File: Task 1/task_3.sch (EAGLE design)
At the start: 6 parts

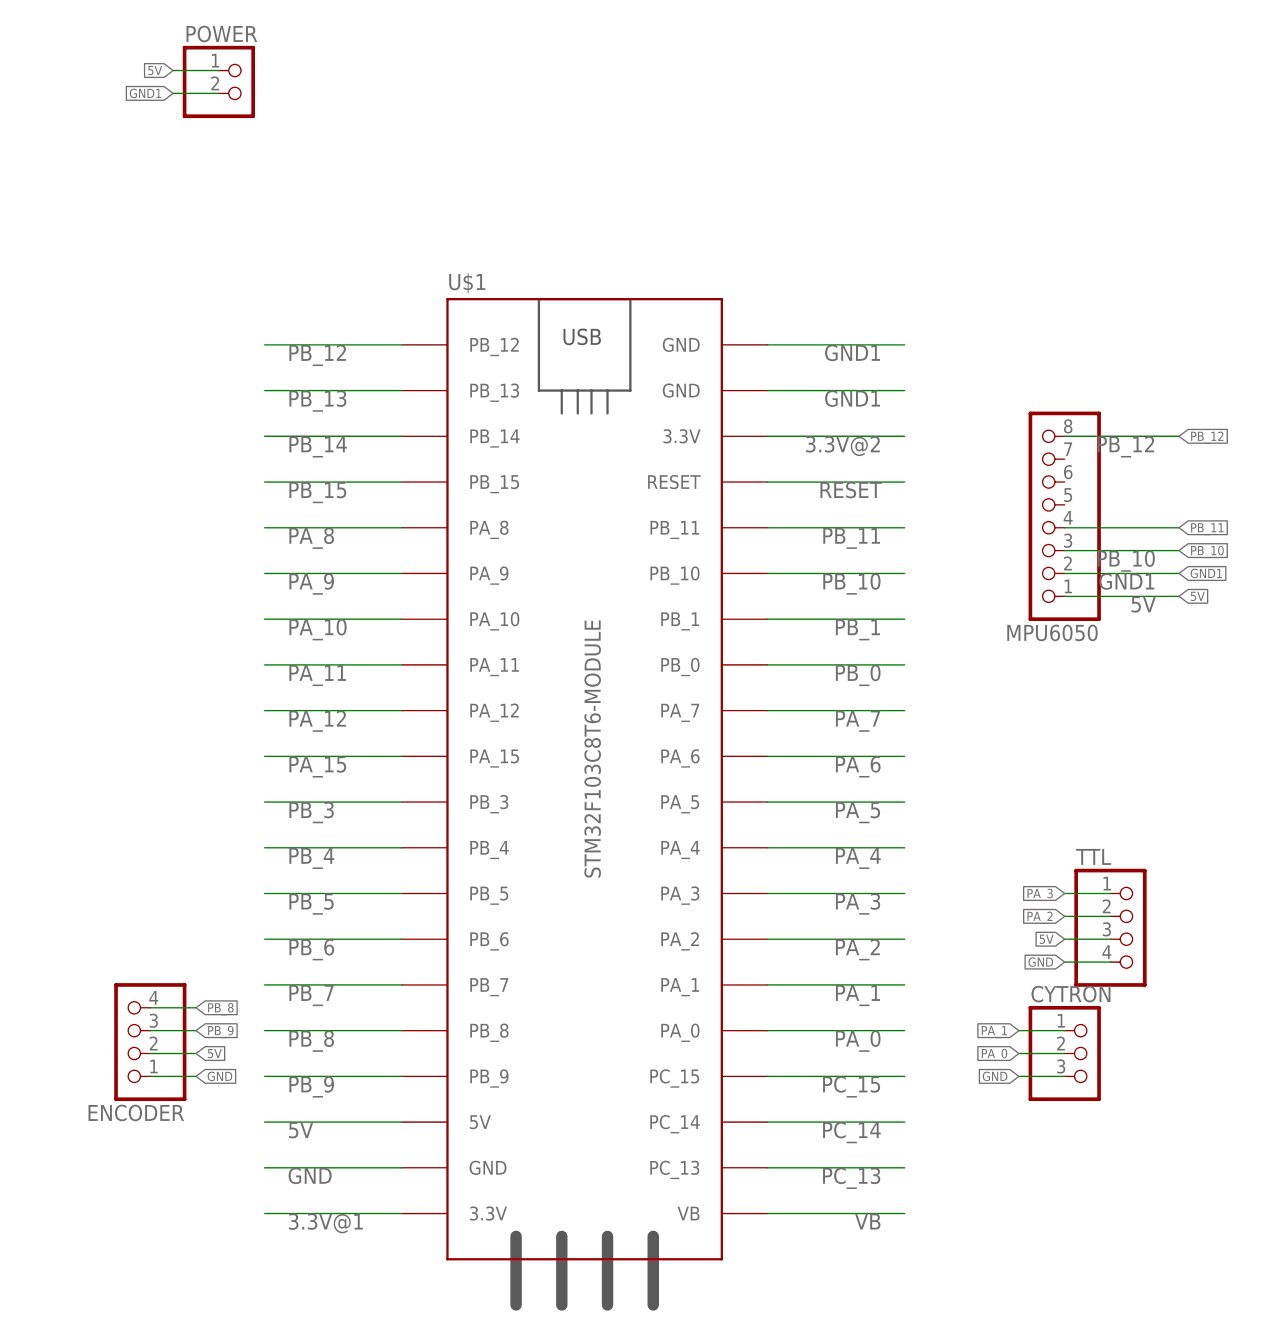
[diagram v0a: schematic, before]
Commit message: added second ttl and used correct data pinheads
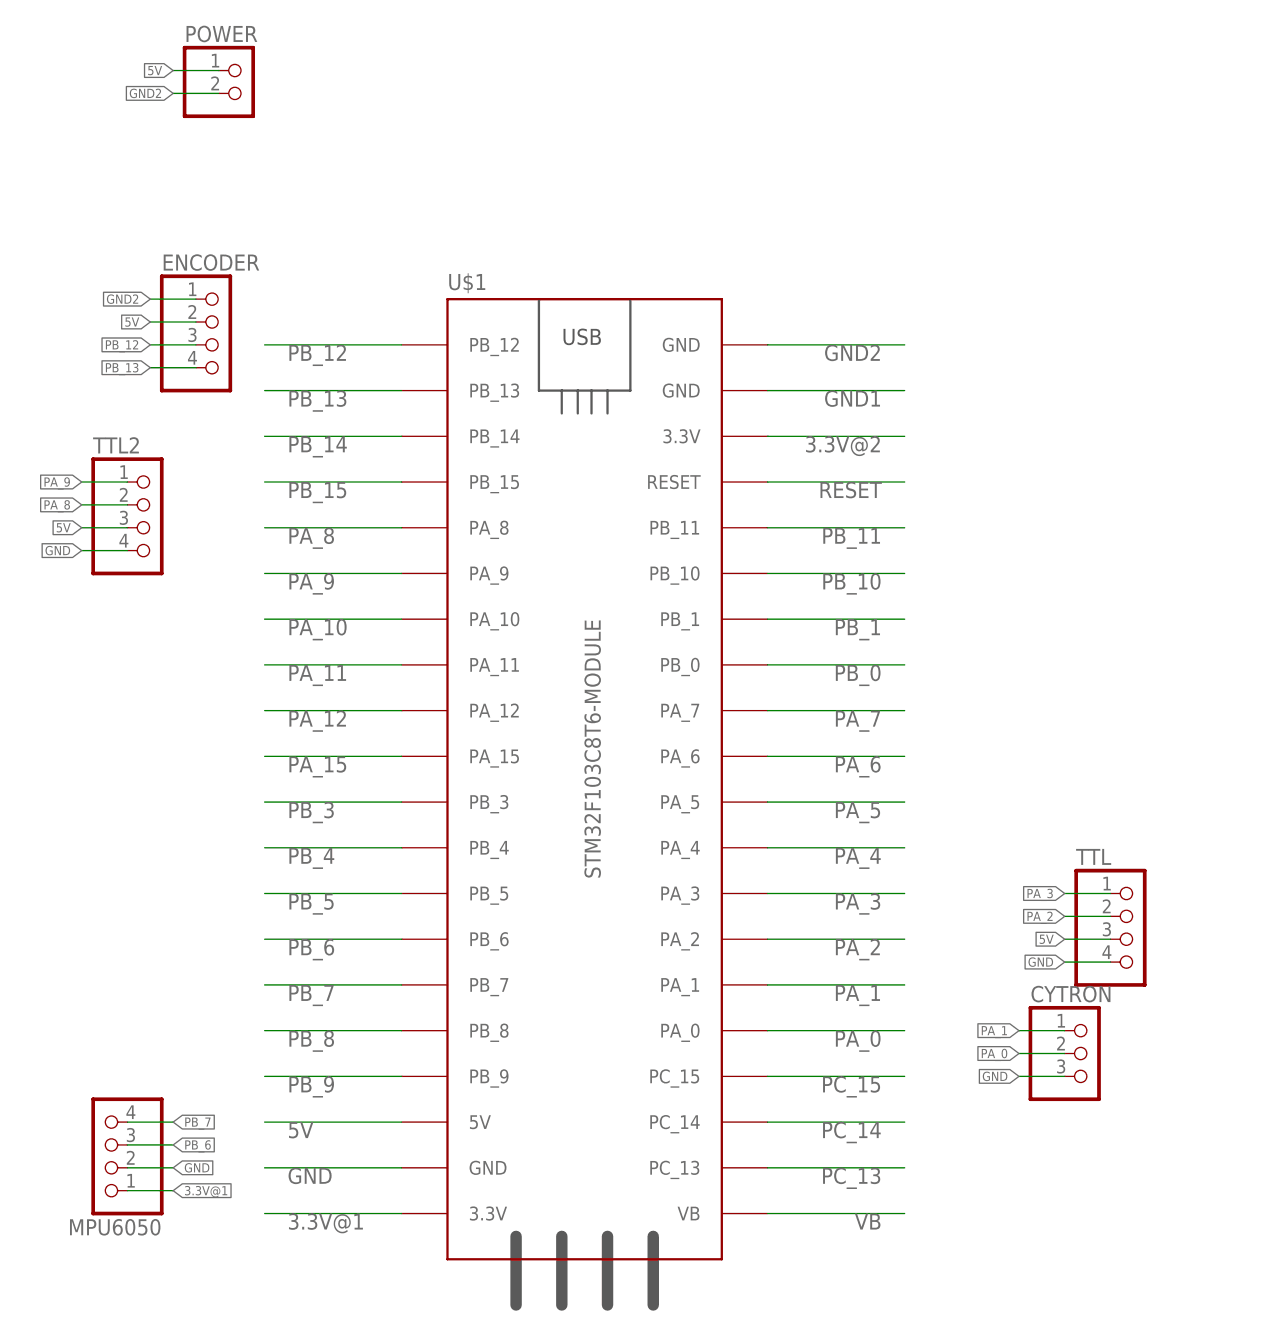
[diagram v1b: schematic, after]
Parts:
- added TTL2: (no value), MIA_LIBRARY-2-2-2:PINHD-4_DATA
- CYTRON: device MIA_LIBRARY-2-2-2:PINHD-1X3 -> MIA_LIBRARY-2-2-2:PINHD-3_DATA
- ENCODER, TTL: device MIA_LIBRARY-2-2-2:PINHD-1X4 -> MIA_LIBRARY-2-2-2:PINHD-4_DATA
- MPU6050: device MIA_LIBRARY-2-2-2:PINHD-1X8 -> MIA_LIBRARY-2-2-2:PINHD-4_DATA
- POWER: device MIA_LIBRARY-2-2-2:PINHD-1X2 -> MIA_LIBRARY-2-2-2:PINHD-2_DATA
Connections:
- new net GND2: ENCODER.1, POWER.2, U$1.GND@3
- net 3.3V@1: now also MPU6050.1
- net 5V: now also TTL2.3; no longer MPU6050.1
- net GND: now also MPU6050.2, TTL2.4; no longer ENCODER.1
- net GND1: no longer MPU6050.2, POWER.2, U$1.GND@3
- net PA_8: now also TTL2.2
- net PA_9: now also TTL2.1
- net PB_10: no longer MPU6050.3
- net PB_11: no longer MPU6050.4
- net PB_12: now also ENCODER.3; no longer MPU6050.8
- net PB_13: now also ENCODER.4
- net PB_6: now also MPU6050.3
- net PB_7: now also MPU6050.4
- net PB_8: no longer ENCODER.4
- net PB_9: no longer ENCODER.3
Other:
- moved on the sheet: ENCODER

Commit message: fixed pin configuration and routing errors, and also updated dimensions and added vias
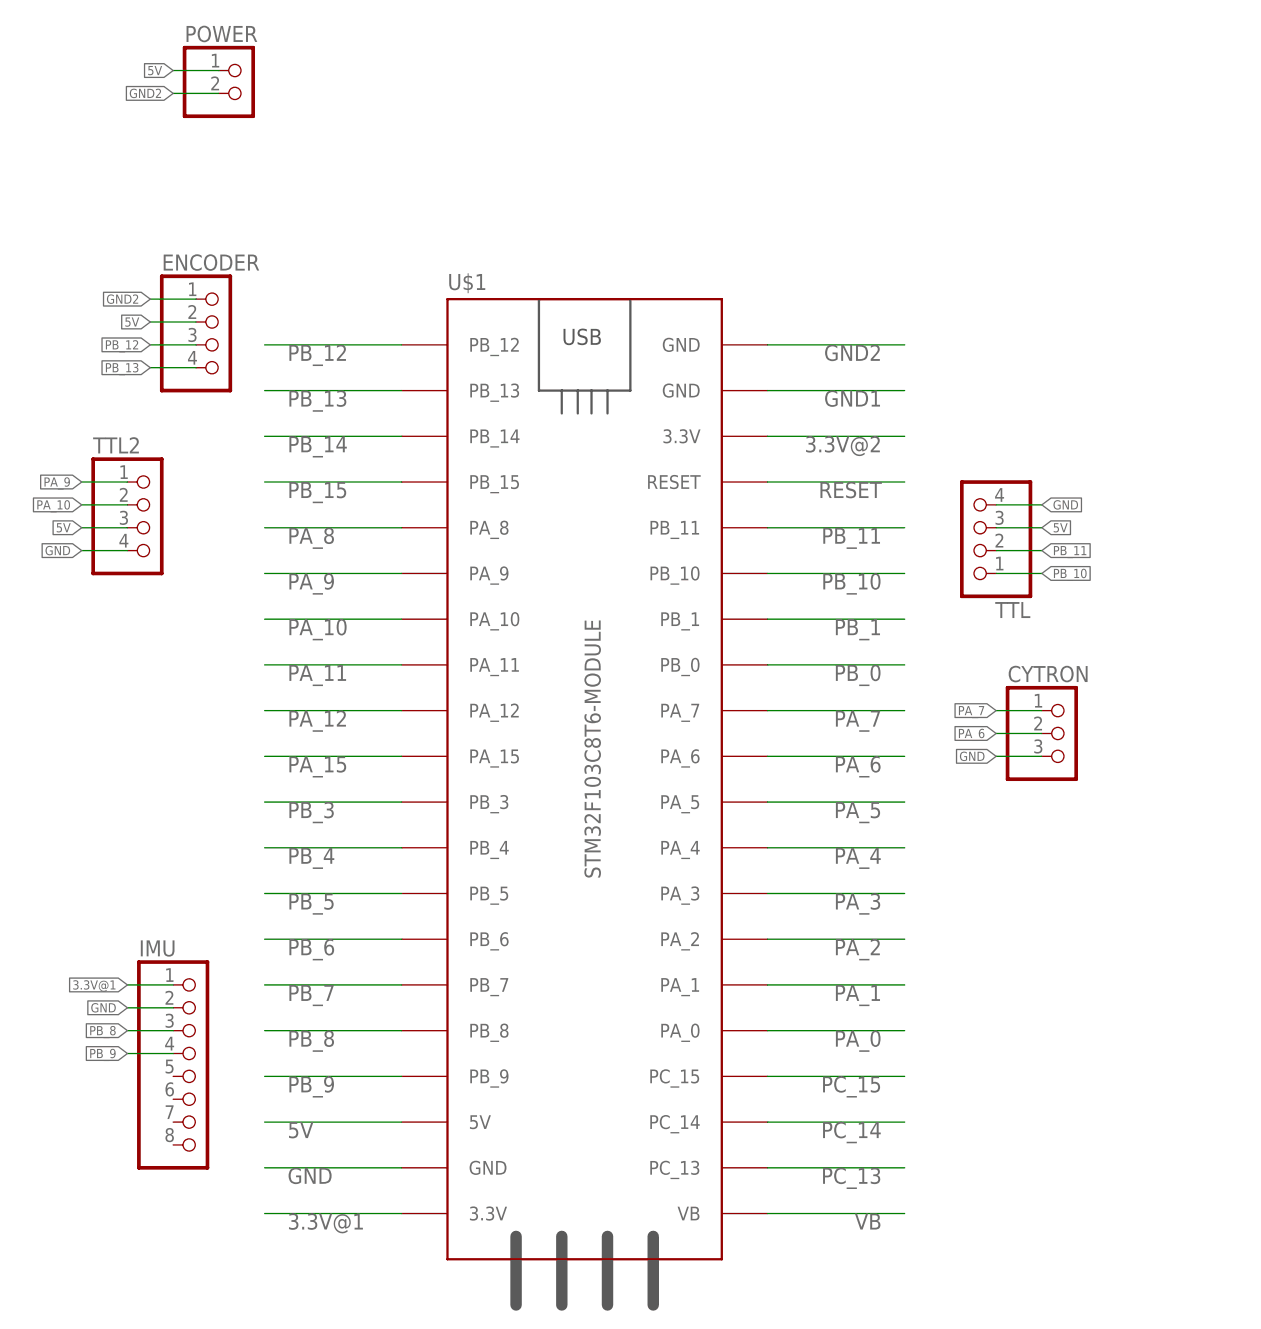
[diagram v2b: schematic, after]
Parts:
- removed MPU6050: (no value), MIA_LIBRARY-2-2-2:PINHD-4_DATA
- added IMU: (no value), MIA_LIBRARY-2-2-2:PINHD-1X8
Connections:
- net 3.3V@1: now also IMU.1; no longer MPU6050.1
- net GND: now also IMU.2; no longer MPU6050.2
- net PA_0: no longer CYTRON.2
- net PA_1: no longer CYTRON.1
- net PA_10: now also TTL2.2
- net PA_2: no longer TTL.2
- net PA_3: no longer TTL.1
- net PA_6: now also CYTRON.2
- net PA_7: now also CYTRON.1
- net PA_8: no longer TTL2.2
- net PB_10: now also TTL.1
- net PB_11: now also TTL.2
- net PB_6: no longer MPU6050.3
- net PB_7: no longer MPU6050.4
- net PB_8: now also IMU.3
- net PB_9: now also IMU.4
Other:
- moved on the sheet: CYTRON, TTL

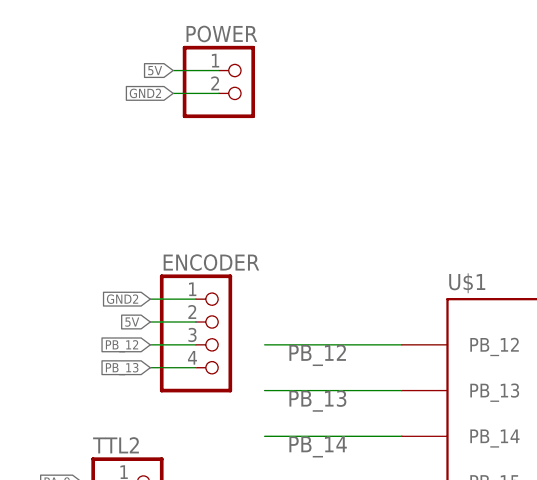
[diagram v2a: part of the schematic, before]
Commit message: ommitted use of jumpers
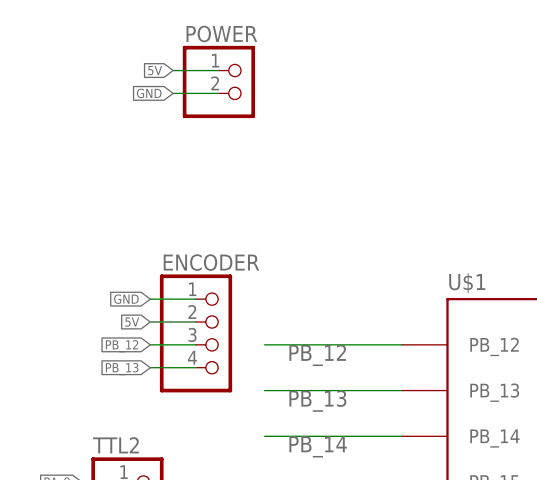
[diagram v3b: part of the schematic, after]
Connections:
- net GND: now also ENCODER.1, POWER.2
- net GND2: no longer ENCODER.1, POWER.2
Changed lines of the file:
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@@
 <label x="127" y="81.28" size="1.016" layer="95" xref="yes"/>
+</segment>
+<segment>
+<pinref part="POWER" gate="G$1" pin="2"/>
+<wire x1="35.56" y1="127" x2="30.48" y2="127" width="0.1524" layer="91"/>
+<label x="30.48" y="127" size="1.016" layer="95" rot="R180" xref="yes"/>
+</segment>
+<segment>
+<pinref part="ENCODER" gate="A" pin="1"/>
+<wire x1="33.02" y1="104.14" x2="27.94" y2="104.14" width="0.1524" layer="91"/>
+<label x="27.94" y="104.14" size="1.016" layer="95" rot="R180" xref="yes"/>
 </segment>
 </net>
@@
 <label x="109.22" y="99.06" size="1.778" layer="95" rot="R180"/>
 </segment>
-<segment>
-<pinref part="ENCODER" gate="A" pin="1"/>
-<wire x1="33.02" y1="104.14" x2="27.94" y2="104.14" width="0.1524" layer="91"/>
-<label x="27.94" y="104.14" size="1.016" layer="95" rot="R180" xref="yes"/>
-</segment>
-<segment>
-<pinref part="POWER" gate="G$1" pin="2"/>
-<wire x1="35.56" y1="127" x2="30.48" y2="127" width="0.1524" layer="91"/>
-<label x="30.48" y="127" size="1.016" layer="95" rot="R180" xref="yes"/>
-</segment>
 </net>
